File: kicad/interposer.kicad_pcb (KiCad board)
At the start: 2 copper layers, 9 parts, among them J1 Conn_Stove, U1 XIAO-nRF52840, U2 Adafruit DS3502, U3 TS5A3159DBV

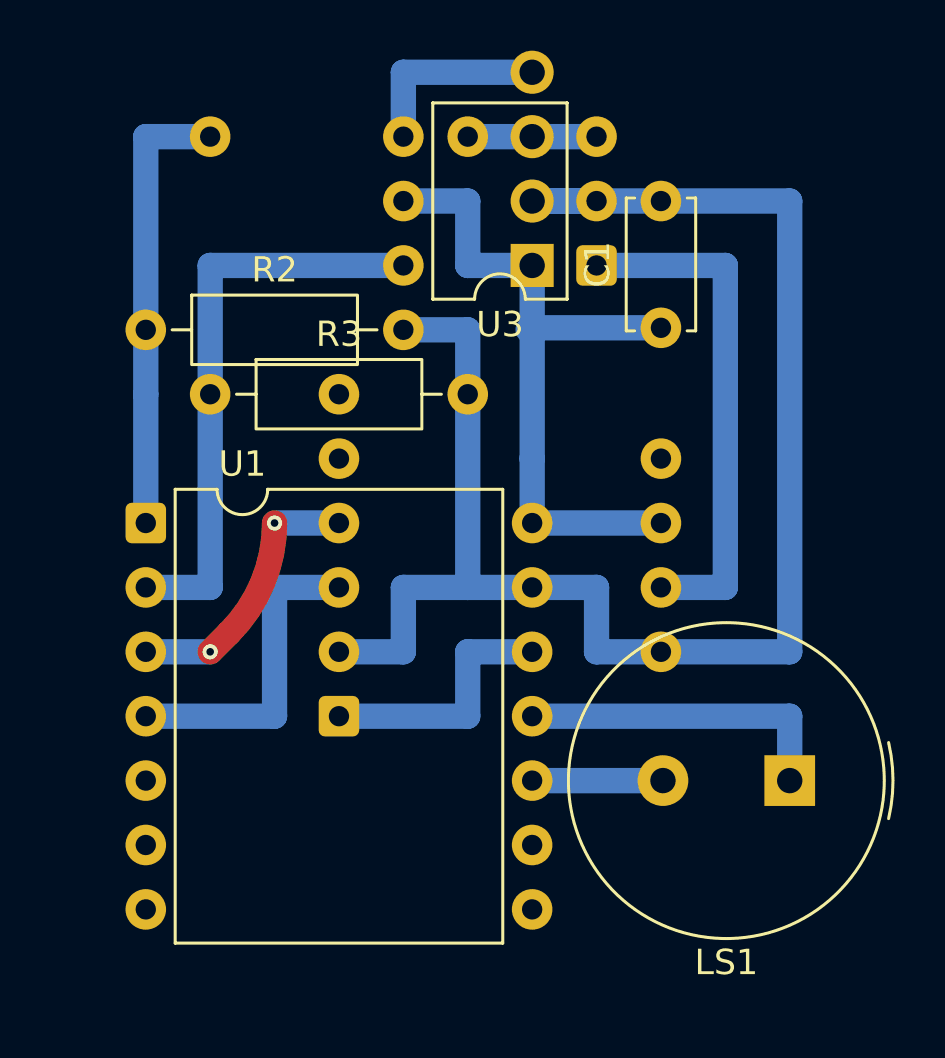
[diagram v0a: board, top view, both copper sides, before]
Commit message: Update KiCad to two layers
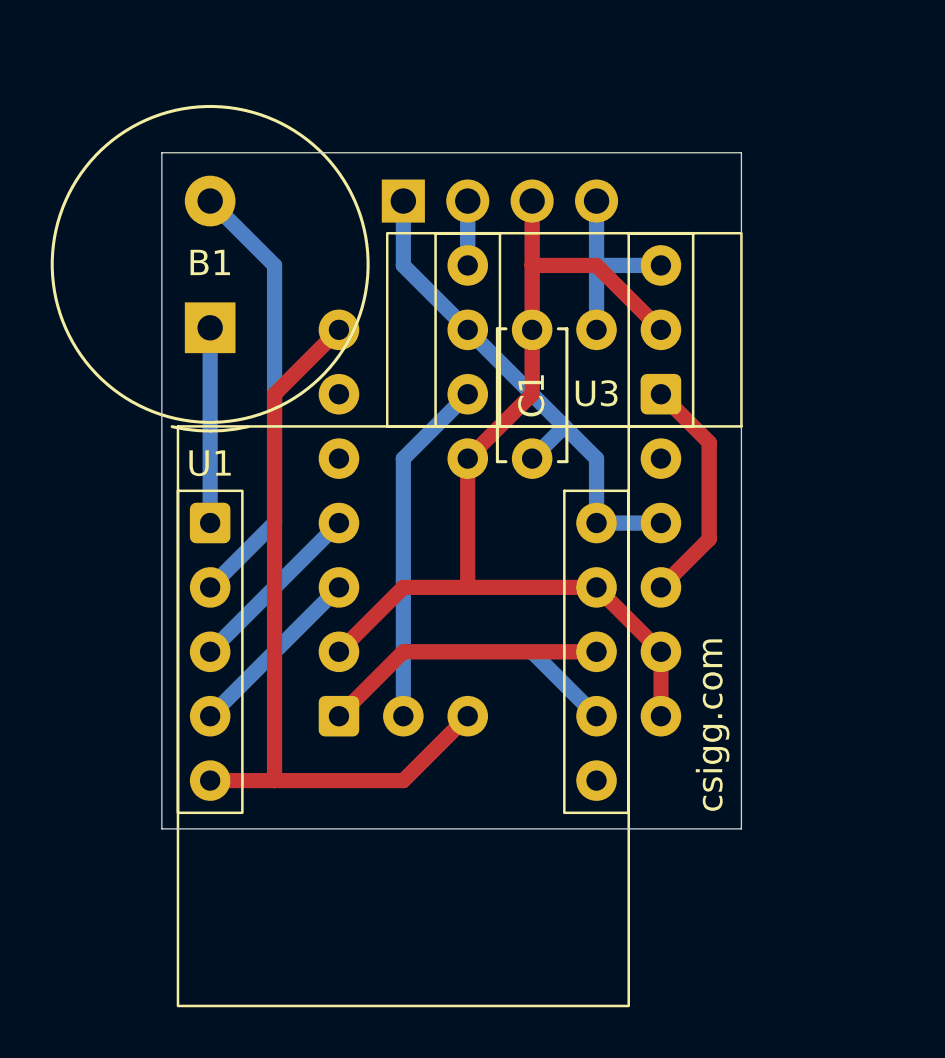
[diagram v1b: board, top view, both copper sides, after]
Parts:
- B1: renamed from LS1; value Speaker -> Buzzer
- R2, R3: moved to B.Cu
- moved B1 29.0 mm to (63.5, 106.6), turned to 90 degrees
- moved R2 19.8 mm to (73.7, 121.9), turned to 90 degrees
- moved R3 14.8 mm to (71.1, 121.9)
- moved R1 9.16 mm to (78.7, 106.7)
- moved C1 7.24 mm to (76.2, 111.8)
- moved J1 5.68 mm to (71.1, 101.6), turned to -90 degrees
- moved U3 5.68 mm to (81.3, 109.2)
- moved U1 2.54 mm to (63.5, 114.3)
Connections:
- B1 pad 1: Net-(U1-PA6_A10_D10_MOSI) -> Net-(U1-PA02_A0_D0)
- B1 pad 2: Net-(U1-PA5_A9_D9_MISO) -> Net-(U1-PA4_A1_D1)
- J1 pad 2: GND -> /RETURN
- J1 pad 3: /KNOB -> GND
- J1 pad 4: /RETURN -> /KNOB
- U1 pad 1: /INPUT -> Net-(U1-PA02_A0_D0)
- U1 pad 10: Net-(U1-PA5_A9_D9_MISO) -> unconnected-(U1-PA5_A9_D9_MISO-Pad10)
- U1 pad 11: Net-(U1-PA6_A10_D10_MOSI) -> /BYPASS
- U1 pad 2: /BYPASS -> Net-(U1-PA4_A1_D1)
- U1 pad 5: unconnected-(U1-PA8_A4_D4_SDA-Pad5) -> /INPUT
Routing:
- net GND: track 66.0 -> 39.8 mm
- net Net-(U1-PA4_A1_D1): track 0.00 -> 17.3 mm
- net Net-(U1-PA6_A10_D10_MOSI): track 12.7 -> 0.00 mm
- net /INPUT: track 17.8 -> 30.0 mm
- net /OUPUT: track 20.3 -> 9.20 mm
- net +5V: track 28.2 -> 20.2 mm
- net Net-(U1-PA02_A0_D0): track 0.00 -> 7.70 mm
- net /SDA: track 12.7 -> 7.18 mm
- net Net-(U1-PA5_A9_D9_MISO): track 5.16 -> 0.00 mm
- net /RETURN: track 7.62 -> 2.54 mm
- net /SCL: track 10.9 -> 7.18 mm, vias 2 -> 0
- net /KNOB: track 5.08 -> 7.62 mm
- net +3V3: track 10.2 -> 11.2 mm
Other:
- board outline added: 22.9 x 26.7 mm
- board text added: "csigg.com"

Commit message: Update KiCad
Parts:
- added C2: 100nF, Capacitor_SMD:C_0805_2012Metric_Pad1.18x1.45mm_HandSolder, B.Cu at (127.7, 88.9)
- added C3: 1µF, Capacitor_SMD:C_0805_2012Metric_Pad1.18x1.45mm_HandSolder, B.Cu at (122.6, 80.1)
- added C4: 1µF, Capacitor_SMD:C_0805_2012Metric_Pad1.18x1.45mm_HandSolder, B.Cu at (123.8, 71.0)
- added J2: Stove, Connector_JST:JST_XH_B3B-XH-A_1x03_P2.50mm_Vertical, F.Cu at (126.2, 73.2)
- added J3: Stove, Connector_JST:JST_XH_S3B-XH-A_1x03_P2.50mm_Horizontal, B.Cu at (124.3, 64.5)
- added Q1: 2N7002, Package_TO_SOT_SMD:SOT-23, B.Cu at (118.7, 91.6)
- added R4: 51kΩ, Resistor_SMD:R_0805_2012Metric_Pad1.20x1.40mm_HandSolder, B.Cu at (127.7, 86.9)
- added R5: 33kΩ, Resistor_SMD:R_0805_2012Metric_Pad1.20x1.40mm_HandSolder, B.Cu at (119.5, 79.6)
- added R6: 100kΩ, Resistor_SMD:R_0805_2012Metric_Pad1.20x1.40mm_HandSolder, F.Cu at (118.4, 86.1)
- added R7: 100Ω, Resistor_SMD:R_0805_2012Metric_Pad1.20x1.40mm_HandSolder, B.Cu at (128.6, 81.3)
- added R8: 1MΩ, Resistor_SMD:R_0805_2012Metric_Pad1.20x1.40mm_HandSolder, B.Cu at (122.3, 93.3)
- added REF**: BreakLine_9h_D0.5mm_P0.85mm, Panelization:BreakLine_9h_D0.5mm_P0.85mm, F.Cu at (121.9, 68.9)
- added U4: TMUX1119DBVR, Package_TO_SOT_SMD:SOT-23-6_Handsoldering, F.Cu at (122.1, 85.9)
- B1: footprint Buzzer_Beeper:Buzzer_TDK_PS1240P02BT_D12.2mm_H6.5mm -> interposer:Buzzer_TDK_PS1240P02BT_D12.2mm_H6.5mm
- C1: value 0.1µF -> 100nF; footprint Capacitor_THT:C_Disc_D5.0mm_W2.5mm_P5.00mm -> Capacitor_SMD:C_0805_2012Metric_Pad1.18x1.45mm_HandSolder
- J1: value Conn_Stove -> Dial; footprint Connector_PinHeader_2.54mm:PinHeader_1x04_P2.54mm_Vertical -> Connector_JST:JST_XH_B3B-XH-A_1x03_P2.50mm_Vertical; moved to F.Cu
- R1: value 10kΩ -> 27kΩ; footprint Resistor_THT:R_Axial_DIN0207_L6.3mm_D2.5mm_P10.16mm_Horizontal -> Resistor_SMD:R_0805_2012Metric_Pad1.20x1.40mm_HandSolder; moved to F.Cu
- R2: value 18kΩ -> 51kΩ; footprint Resistor_THT:R_Axial_DIN0207_L6.3mm_D2.5mm_P10.16mm_Horizontal -> Resistor_SMD:R_0805_2012Metric_Pad1.20x1.40mm_HandSolder; moved to F.Cu
- R3: value 10kΩ -> 27kΩ; footprint Resistor_THT:R_Axial_DIN0207_L6.3mm_D2.5mm_P10.16mm_Horizontal -> Resistor_SMD:R_0805_2012Metric_Pad1.20x1.40mm_HandSolder
- U1: value XIAO-nRF52840 -> XIAO-nRF52840-DIP; footprint Package_DIP:DIP-14_W7.62mm -> interposer:XIAO-nRF52840-DIP; moved to B.Cu
- U2: value Adafruit DS3502 -> MCP6042-E_SN; footprint Package_DIP:DIP-12_W7.62mm -> Package_SO:SOIC-8_3.9x4.9mm_P1.27mm
- U3: value TS5A3159DBV -> TXU0101DBVR; footprint Package_DIP:DIP-6_W7.62mm -> Package_TO_SOT_SMD:SOT-23-6_Handsoldering; moved to B.Cu
- moved R2 68.0 mm to (128.9, 82.3)
- moved R3 67.7 mm to (127.7, 84.8)
- moved B1 67.3 mm to (126.2, 82.2), turned to 180 degrees
- moved U1 64.8 mm to (123.7, 90.3), turned to 90 degrees
- moved U2 64.0 mm to (122.0, 86.7), turned to 180 degrees
- moved C1 58.2 mm to (128.0, 85.2), turned to 180 degrees
- moved U3 53.1 mm to (123.7, 77.3)
- moved R1 53.0 mm to (128.0, 87.2), turned to 0 degrees
- moved J1 51.4 mm to (121.4, 91.2), turned to 0 degrees
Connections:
- B1 pad 1: Net-(U1-PA02_A0_D0) -> Net-(B1-Pad1)
- B1 pad 2: Net-(U1-PA4_A1_D1) -> /-BUZZ
- C1 pad 1: +5V -> /REF
- J1 pad 2: /RETURN -> /DIAL
- R1 pad 1: /KNOB -> +5V
- R1 pad 2: /INPUT -> /REF
- R2 pad 1: /INPUT -> /REF
- R3 pad 1: /BYPASS -> /IN
- R3 pad 2: GND -> /READ
- U1 pad 1: Net-(U1-PA02_A0_D0) -> /PWM_3V3
- U1 pad 11: /BYPASS -> /SEL
- U1 pad 14: +5V -> unconnected-(U1-VBUS-Pad14)
- U1 pad 2: Net-(U1-PA4_A1_D1) -> /+BUZZ
- U1 pad 3: /SCL -> /-BUZZ
- U1 pad 4: /SDA -> /READ
- U1 pad 5: /INPUT -> /REF
- U2 pad 1: /SCL -> /IN
- U2 pad 2: GND -> /IN
- U2 pad 3: +3V3 -> /DIAL
- U2 pad 4: unconnected-(U2-A1-Pad4) -> GND
- U2 pad 5: unconnected-(U2-A0-Pad5) -> /RC
- U2 pad 6: +5V -> /OUT
- U2 pad 7: /OUPUT -> /OUT
- U2 pad 8: GND -> +5V
- U3 pad 1: /OUPUT -> +3V3
- U3 pad 3: /KNOB -> /PWM_3V3
- U3 pad 4: /RETURN -> /PWM_5V
- U3 pad 5: +5V -> +3V3
- U3 pad 6: /BYPASS -> +5V
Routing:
- net GND: track 39.8 -> 74.0 mm, vias 0 -> 1
- net /INPUT: track 30.0 -> 0.00 mm
- net /BYPASS: track 22.4 -> 0.00 mm
- net +5V: track 20.2 -> 39.1 mm, vias 0 -> 1
- net Net-(U1-PA4_A1_D1): track 17.3 -> 0.00 mm
- net /-BUZZ: track 0.00 -> 13.7 mm
- net /STOVE: track 0.00 -> 12.7 mm
- net /DIAL: track 0.00 -> 11.1 mm, vias 0 -> 1
- net /RC: track 0.00 -> 11.1 mm
- net /REF: track 0.00 -> 10.5 mm
- net /OUPUT: track 9.20 -> 0.00 mm
- net /PWM_3V3: track 0.00 -> 9.18 mm
- net /SEL: track 0.00 -> 8.65 mm
- net Net-(U1-PA02_A0_D0): track 7.70 -> 0.00 mm
- net /KNOB: track 7.62 -> 0.00 mm
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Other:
- board size 22.9 x 26.7 mm -> 18.3 x 39.7 mm
- board text added: "Conn_Internal"
- board text added: "DIAL"
- board text added: "STOVE"
